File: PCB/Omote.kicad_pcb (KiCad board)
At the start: 2 copper layers, 192.4 x 50 mm, 158 parts, among them J1 USB_C_Receptacle_USB2.0, J2 Conn_01x50, J3 JST_PH_B2B-PH, J4 2.54x2 Header, Q1 DMG2301L, Q2 MBT3904DW1, Q3 DMG2301L, Q4 DMG2301L, Q5 DMG2301L, Q6 FS8205A, U1 DW01A, U10 APX803S, U11 TP4056, U2 XC6220B331, U3 CH340C, U4 USBLC6-2P6, U5 LIS3DHTR, U6 TSSP77038, U7 ESP32-PICO-D4, U8 AP2112K-3.3, U9 MAX17048G

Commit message: REV5 hardware added
TODO: update production files and BOMs
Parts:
- removed AE1: Antenna, omoteLib:RFANT5220110A2T
- removed C19: 1.2pF, Capacitor_SMD:C_0603_1608Metric
- removed kibuzzard-643EE532: G***, kibuzzard-643EE532
- removed kibuzzard-643EE5A3: G***, kibuzzard-643EE5A3
- added C29: 100nF, Capacitor_SMD:C_0603_1608Metric, F.Cu at (120.2, 116.9)
- added D10: LED, LED_SMD:LED_0603_1608Metric, B.Cu at (152.8, 91.9)
- added D11: LED, LED_SMD:LED_0603_1608Metric, B.Cu at (173.1, 91.8)
- added D12: LED, LED_SMD:LED_0603_1608Metric, B.Cu at (199.4, 117.0)
- added D13: LED, LED_SMD:LED_0603_1608Metric, B.Cu at (199.4, 102.0)
- added D14: LED, LED_SMD:LED_0603_1608Metric, B.Cu at (199.4, 87.0)
- added D15: LED, LED_SMD:LED_0603_1608Metric, B.Cu at (136.4, 102.0)
- added D16: LED, LED_SMD:LED_0603_1608Metric, B.Cu at (57.8, 124.2)
- added D6: LED, LED_SMD:LED_0603_1608Metric, B.Cu at (136.4, 89.7)
- added D7: LED, LED_SMD:LED_0603_1608Metric, B.Cu at (136.4, 114.3)
- added D8: LED, LED_SMD:LED_0603_1608Metric, B.Cu at (152.9, 112.0)
- added D9: LED, LED_SMD:LED_0603_1608Metric, B.Cu at (173.1, 112.0)
- added J5: Micro_SD_Card, omoteLib:MicroSD Slot TF-01A, F.Cu at (76.0, 116.0)
- added Q7: DMG2301L, Package_TO_SOT_SMD:SOT-23, F.Cu at (73.8, 105.2)
- added R10: 10k, Resistor_SMD:R_0603_1608Metric, F.Cu at (120.2, 115.4)
- added R2: 330, Resistor_SMD:R_0603_1608Metric, F.Cu at (72.8, 101.0)
- added R24: 10k, Resistor_SMD:R_0603_1608Metric, F.Cu at (72.8, 102.5)
- added R38: 2k2, Resistor_SMD:R_0603_1608Metric, B.Cu at (173.1, 93.3)
- added R41: 2k2, Resistor_SMD:R_0603_1608Metric, B.Cu at (199.4, 115.5)
- added R42: 2k2, Resistor_SMD:R_0603_1608Metric, B.Cu at (199.4, 100.5)
- added R43: 2k2, Resistor_SMD:R_0603_1608Metric, B.Cu at (199.4, 85.5)
- added R44: 2k2, Resistor_SMD:R_0603_1608Metric, F.Cu at (57.0, 123.2)
- added TP14: TestPoint, TestPoint:TestPoint_Pad_D1.5mm, F.Cu at (126.0, 112.5)
- added TP15: TestPoint, TestPoint:TestPoint_Pad_D1.5mm, F.Cu at (123.3, 112.5)
- added TP16: TestPoint, TestPoint:TestPoint_Pad_D1.5mm, F.Cu at (120.6, 112.5)
- added TP17: TestPoint, TestPoint:TestPoint_Pad_D1.5mm, B.Cu at (78.5, 108.7)
- added TP18: TestPoint, TestPoint:TestPoint_Pad_D1.5mm, B.Cu at (77.8, 111.2)
- added TP19: TestPoint, TestPoint:TestPoint_Pad_D1.5mm, B.Cu at (73.8, 108.7)
- added TP20: TestPoint, TestPoint:TestPoint_Pad_D1.5mm, B.Cu at (70.2, 110.0)
- added TP21: TestPoint, TestPoint:TestPoint_Pad_D1.5mm, B.Cu at (68.0, 121.2)
- added TP22: TestPoint, TestPoint:TestPoint_Pad_D1.5mm, B.Cu at (60.9, 124.2)
- added TP23: TestPoint, TestPoint:TestPoint_Pad_D1.5mm, B.Cu at (74.9, 111.5)
- added U12: TCA8418, Package_DFN_QFN:HVQFN-24-1EP_4x4mm_P0.5mm_EP2.5x2.5mm, F.Cu at (124.8, 118.1)
- C11: value 2.2uF -> 10uF; footprint Capacitor_SMD:C_0603_1608Metric -> Capacitor_SMD:C_0805_2012Metric
- C14: value 100nF -> 10uF; footprint Capacitor_SMD:C_0603_1608Metric -> Capacitor_SMD:C_0805_2012Metric
- C18: value 1.2pF -> 10uF; footprint Capacitor_SMD:C_0603_1608Metric -> Capacitor_SMD:C_0805_2012Metric
- D1: value MBR0520 -> BAT20J; footprint Diode_SMD:D_SOD-123 -> Diode_SMD:D_SOD-323
- D2: value SFH4547 -> SFH4547
- H4: footprint MountingHole:MountingHole_3.2mm_M3_Pad_Via -> MountingHole:MountingHole_3.2mm_M3
- R23, R31, R32, R33, R34, R35: value 10k -> 2k2; moved to B.Cu
- R36: value 0 -> 10k
- U7: value ESP32-PICO-D4 -> ESP32-S3-WROOM-1-N16R8; footprint omoteLib:QFN-48-1EP_7x7mm_P0.5mm_EP5.3x5.3mm_ThermalVias_MR -> RF_Module:ESP32-S3-WROOM-1
- moved R23 56.5 mm to (133.4, 102.0), turned to 0 degrees
- moved C14 51.6 mm to (116.8, 108.3), turned to -90 degrees
- moved FID4 43.4 mm to (54.7, 122.3)
- moved R34 42.0 mm to (173.1, 110.5)
- moved R31 35.4 mm to (133.4, 89.7)
- moved TP4 34.8 mm to (65.6, 80.6)
- moved FID3 34.7 mm to (239.4, 85.0)
- moved R35 32.7 mm to (152.8, 93.4), turned to 180 degrees
- moved TP3 32.6 mm to (67.9, 79.3)
- moved G*** 30.0 mm to (92.5, 117.8)
- moved R33 23.7 mm to (152.9, 110.5), turned to 180 degrees
- moved TP8 22.7 mm to (78.2, 105.8)
- moved R5 21.1 mm to (84.8, 82.5), turned to 180 degrees
- moved D3 20.5 mm to (81.7, 82.5)
- moved kibuzzard-643EE5B9 20.0 mm to (59.0, 122.8)
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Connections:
- net Net-(U3-V3) renamed USB_3V3
- C11 pad 1: +3.3V -> GND
- C11 pad 2: GND -> +3.3V
- C14 pad 1: +3.3V -> GND
- C14 pad 2: GND -> SW_BL
- C18 pad 2: Net-(U7-LNA_IN) -> /SD_3V3
- J2 pad 11: GND -> unconnected-(J2-Pin_11-Pad11)
- J2 pad 12: GND -> unconnected-(J2-Pin_12-Pad12)
- J2 pad 13: GND -> unconnected-(J2-Pin_13-Pad13)
- J2 pad 14: GND -> unconnected-(J2-Pin_14-Pad14)
- J2 pad 25: GND -> LCD_D7
- J2 pad 26: GND -> LCD_D6
- J2 pad 27: GND -> LCD_D5
- J2 pad 28: GND -> LCD_D4
- J2 pad 29: GND -> LCD_D3
- J2 pad 30: GND -> LCD_D2
- J2 pad 31: GND -> LCD_D1
- J2 pad 32: GND -> LCD_D0
- J2 pad 34: LCD_MOSI -> unconnected-(J2-Pin_34-Pad34)
- J2 pad 35: unconnected-(J2-Pin_35-Pad35) -> LCD_RD
- J2 pad 36: LCD_DC -> LCD_WR
- J2 pad 37: LCD_SCK -> LCD_DC
- J2 pad 7: +VSW -> GND
- J2 pad 8: +VSW -> GND
- J2 pad 9: +VSW -> GND
- R23 pad 1: CRG_STAT -> GND
- R23 pad 2: +3.3V -> Net-(D15-K)
- R31 pad 1: SW_A -> GND
- R31 pad 2: GND -> Net-(D6-K)
- R32 pad 1: SW_B -> GND
- R32 pad 2: GND -> Net-(D7-K)
- R33 pad 1: SW_C -> GND
- R33 pad 2: GND -> Net-(D8-K)
- R34 pad 1: SW_D -> GND
- R34 pad 2: GND -> Net-(D9-K)
- R35 pad 1: SW_E -> GND
- R35 pad 2: GND -> Net-(D10-K)
- R36 pad 1: Net-(AE1-A) -> TCA_INT
- R36 pad 2: Net-(U7-LNA_IN) -> +3.3V
- S17 pad 1: SW_2 -> GND
- S17 pad 2: SW_D -> SW_PWR
- U7 pad 1: +3.3V -> GND
- U7 pad 10: SW_D -> SD_MOSI
- U7 pad 11: SW_E -> SD_CS
- U7 pad 12: SW_1 -> TCA_INT
- U7 pad 13: IR_LED -> SCL
- U7 pad 14: IR_VCC -> SDA
- U7 pad 15: SW_2 -> unconnected-(U7-IO3-Pad15)
- U7 pad 16: SW_3 -> SW_BL
- U7 pad 17: SW_4 -> LCD_BL
- U7 pad 18: SW_5 -> LCD_D7
- U7 pad 19: +3.3V -> LCD_D6
- U7 pad 2: Net-(U7-LNA_IN) -> +3.3V
- U7 pad 20: ACC_INT -> LCD_D5
- U7 pad 21: IR_RX -> LCD_D4
- U7 pad 22: Net-(D3-A) -> LCD_D3
- U7 pad 23: IO0 -> LCD_D2
- U7 pad 24: LCD_BL -> LCD_D1
- U7 pad 25: unconnected-(U7-IO16-Pad25) -> LCD_D0
- U7 pad 26: unconnected-(U7-VDD_SDIO-Pad26) -> Net-(D3-A)
- U7 pad 27: unconnected-(U7-IO17-Pad27) -> IO0
- U7 pad 28: LCD_DC -> unconnected-(U7-IO35-Pad28)
- U7 pad 29: LCD_EN -> unconnected-(U7-IO36-Pad29)
- U7 pad 3: +3.3V -> ESP_EN
- U7 pad 31: unconnected-(U7-CLK-Pad31) -> LCD_EN
- U7 pad 32: unconnected-(U7-SD0-Pad32) -> LCD_CS
- U7 pad 33: unconnected-(U7-SD1-Pad33) -> LCD_DC
- U7 pad 34: LCD_CS -> LCD_WR
- U7 pad 35: LCD_SCK -> LCD_RD
- U7 pad 36: LCD_MOSI -> USB_RXD
- U7 pad 37: +3.3V -> USB_TXD
- U7 pad 38: SDA -> ACC_INT
- U7 pad 39: SCL -> CRG_STAT
- U7 pad 4: +3.3V -> IR_RX
- U7 pad 40: USB_RXD -> GND
- U7 pad 41: USB_TXD -> GND
- U7 pad 5: unconnected-(U7-SENSOR_VP-Pad5) -> IR_LED
- U7 pad 6: SW_A -> IR_VCC
- U7 pad 7: SW_B -> SD_MISO
- U7 pad 8: SW_C -> SD_SCK
- U7 pad 9: ESP_EN -> SD_EN
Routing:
- net SW_BL: track 0.00 -> 343.4 mm, vias 0 -> 5
- net USB_3V3: track 18.9 -> 123.3 mm, vias 0 -> 2
- net SW_D: track 171.7 -> 73.8 mm, vias 2 -> 1
- net SW_2: track 173.8 -> 80.4 mm, vias 2 -> 1
- net SW_C: track 232.7 -> 145.0 mm
- net SW_B: track 167.9 -> 81.6 mm
- net SW_A: track 211.6 -> 126.6 mm
- net SW_E: track 135.9 -> 55.9 mm
- net SW_1: track 159.4 -> 84.3 mm
- net SW_3: track 169.4 -> 95.6 mm
- net SD_DET: track 0.00 -> 71.4 mm, vias 0 -> 1
- net SW_PWR: track 0.00 -> 69.9 mm, vias 0 -> 1
- net SW_4: track 167.3 -> 97.7 mm
- net SW_5: track 187.4 -> 120.9 mm
- net SCL: track 178.5 -> 244.9 mm, vias 3 -> 5
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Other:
- outline, holes or cut-outs redrawn
- board text added: "OMOTE Rev. 5 Maximilian Kern 12/2024"
- board text removed: "OMOTE Rev. 4 Maximilian Kern 04/2024"

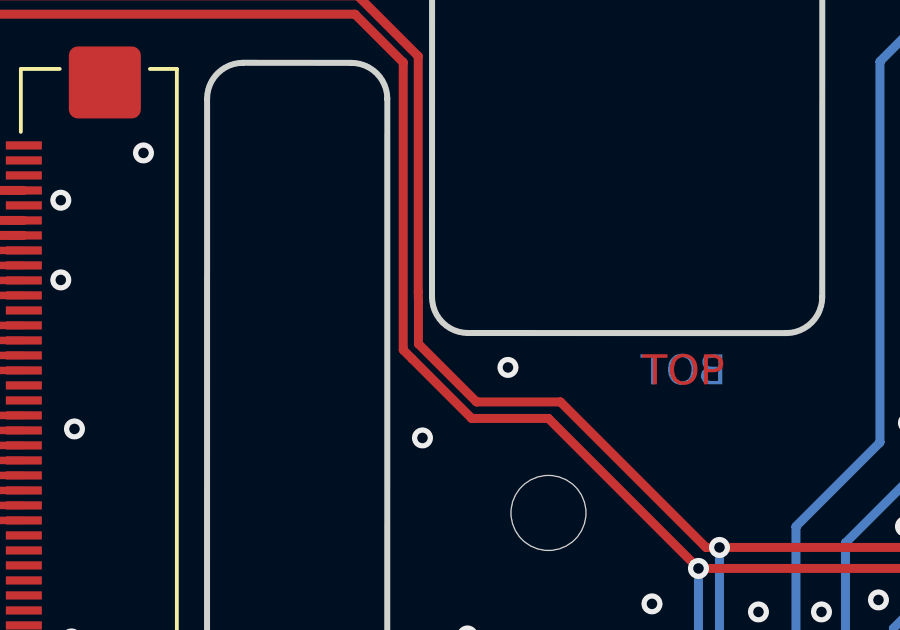
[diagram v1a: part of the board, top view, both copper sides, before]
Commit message: Fixed LCSC number for R7/R9
The LCSC part number  for R7 and R9 was wrongly linked to a 5.1 Ohm resistor instead of a 5.1 KiloOhm resistor.
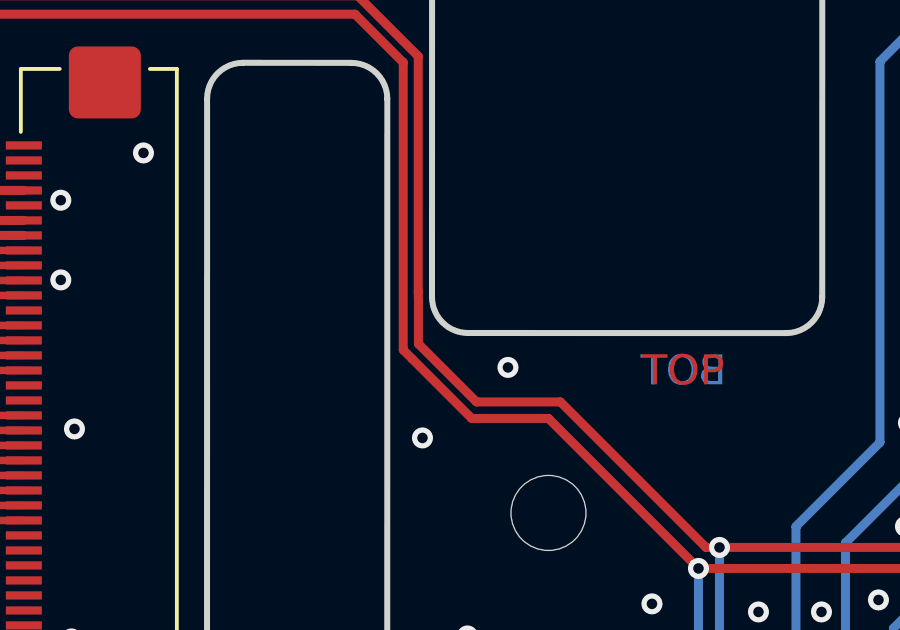
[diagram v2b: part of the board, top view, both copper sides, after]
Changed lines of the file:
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@@
 		(fp_arc
 			(start 5.997926 25.19481)
-			(mid 6.349398 24.346284)
+			(mid 6.349398 24.34628)
 			(end 7.197926 23.99481)
 			(stroke
@@
 			(pinfunction "1")
 			(pintype "input")
+			(zone_connect 2)
 		)
 		(pad "1" thru_hole circle
@@
 			)
 		)
-		(property "LCSC" "C114626"
+		(property "LCSC" "C105580"
 			(at 0 0 90)
 			(unlocked yes)
@@
 			)
 		)
-		(property "LCSC" "C114626"
+		(property "LCSC" "C105580"
 			(at 0 0 0)
 			(unlocked yes)
@@
 			)
 		)
-		(property "LCSC" "C965807"
+		(property "LCSC" "C84265"
 			(at 0 0 180)
 			(unlocked yes)
@@
 			)
 		)
-		(property "LCSC" "C965807"
+		(property "LCSC" "C84265"
 			(at 0 0 0)
 			(unlocked yes)
@@
 			)
 		)
-		(property "LCSC" "C965807"
+		(property "LCSC" "C84265"
 			(at 0 0 0)
 			(unlocked yes)
@@
 			)
 		)
-		(property "LCSC" "C965807"
+		(property "LCSC" "C84265"
 			(at 0 0 180)
 			(unlocked yes)
@@
 			)
 		)
-		(property "LCSC" "C965807"
+		(property "LCSC" "C84265"
 			(at 0 0 180)
 			(unlocked yes)
@@
 			)
 		)
-		(property "LCSC" "C965807"
+		(property "LCSC" "C84265"
 			(at 0 0 0)
 			(unlocked yes)
@@
 			)
 		)
-		(property "LCSC" "C965807"
+		(property "LCSC" "C84265"
 			(at 0 0 180)
 			(unlocked yes)
@@
 			)
 		)
-		(property "LCSC" "C965807"
+		(property "LCSC" "C84265"
 			(at 0 0 0)
 			(unlocked yes)
@@
 			)
 		)
-		(property "LCSC" "C965807"
+		(property "LCSC" "C84265"
 			(at 0 0 180)
 			(unlocked yes)
@@
 			)
 		)
-		(property "LCSC" "C965807"
+		(property "LCSC" "C84265"
 			(at 0 0 0)
 			(unlocked yes)
@@
 			)
 		)
-		(property "LCSC" "C965807"
+		(property "LCSC" "C84265"
 			(at 0 0 180)
 			(unlocked yes)

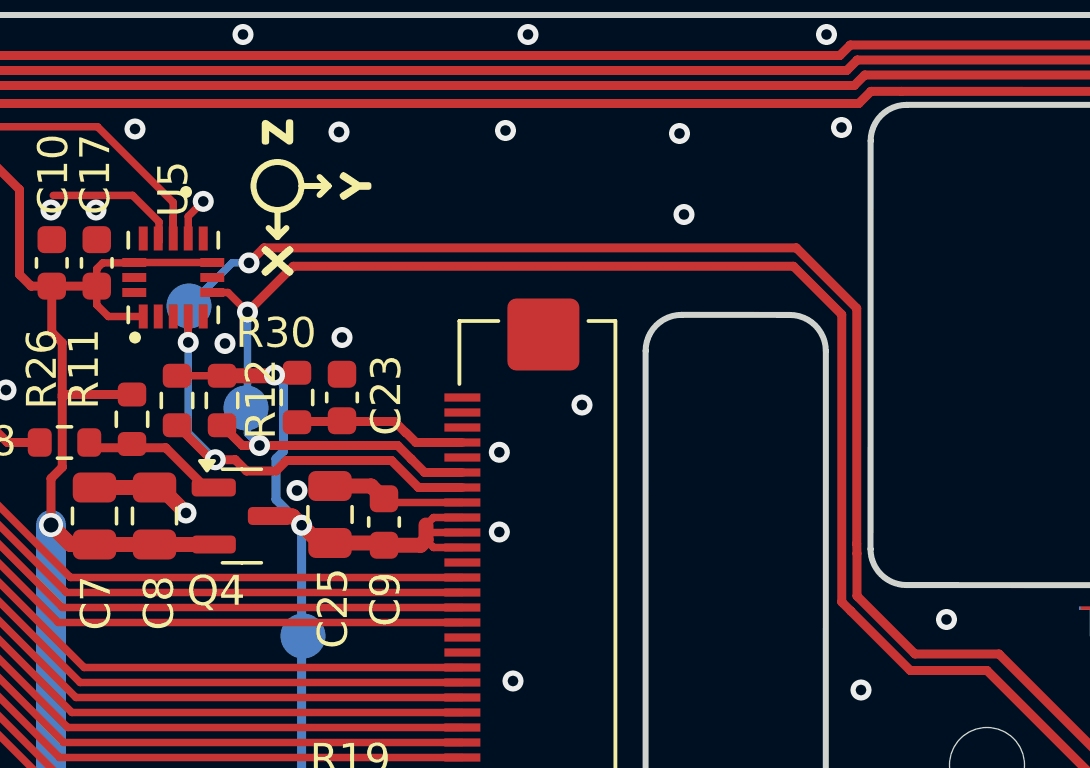
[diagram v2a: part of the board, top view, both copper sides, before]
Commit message: MOSFET circuit adjustment
- Increased gate resistors from 330Ohm to 1kOhm to lower edge speeds slightly (not absolutely necessary but 1k seems to be a default value for most display eval boards)
- Set R25 (gate pull-up for backlight) to 10kOhm like all others
- Removed C14 to reduce load on the ESP32 pin
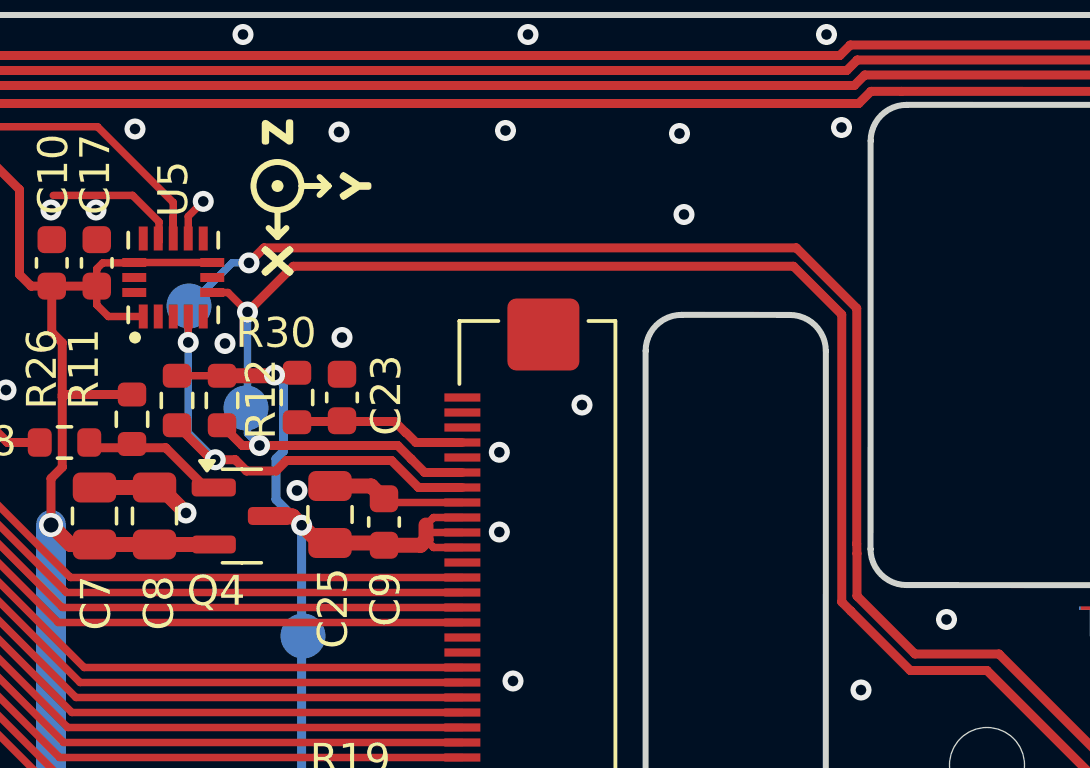
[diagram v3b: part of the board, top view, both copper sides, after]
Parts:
- R2, R27, R28, R29: value 330 -> 1k
- R25: value 4k7 -> 10k
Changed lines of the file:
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@@
 			)
 		)
-		(property "Value" "4k7"
+		(property "Value" "10k"
 			(at 0 1.43 0)
 			(layer "F.Fab")
@@
 			)
 		)
-		(property "LCSC" "C99782"
+		(property "LCSC" "C98220"
 			(at 0 0 180)
 			(unlocked yes)
@@
 		(sheetname "Root")
 		(sheetfile "Omote.kicad_sch")
+		(zone_connect 2)
 		(attr exclude_from_pos_files exclude_from_bom)
 		(fp_circle
@@
 		(fp_arc
 			(start 5.997926 25.19481)
-			(mid 6.349398 24.34628)
+			(mid 6.349398 24.346284)
 			(end 7.197926 23.99481)
 			(stroke
@@
 		(sheetname "Root")
 		(sheetfile "Omote.kicad_sch")
-		(attr smd)
+		(attr smd exclude_from_bom dnp)
 		(fp_line
 			(start -0.261252 0.735)
@@
 			)
 		)
-		(property "Value" "330"
+		(property "Value" "1k"
 			(at 0 1.43 0)
 			(layer "F.Fab")
@@
 			)
 		)
-		(property "LCSC" "C105881"
+		(property "LCSC" "C22548"
 			(at 0 0 0)
 			(unlocked yes)
@@
 			)
 		)
-		(property "Value" "330"
+		(property "Value" "1k"
 			(at 0 1.43 0)
 			(layer "F.Fab")
@@
 			)
 		)
-		(property "LCSC" "C105881"
+		(property "LCSC" "C22548"
 			(at 0 0 180)
 			(unlocked yes)
@@
 		(sheetname "Root")
 		(sheetfile "Omote.kicad_sch")
+		(zone_connect 2)
 		(attr exclude_from_pos_files exclude_from_bom)
 		(fp_circle
@@
 			)
 		)
-		(property "Value" "330"
+		(property "Value" "1k"
 			(at 0 1.43 0)
 			(layer "F.Fab")
@@
 			)
 		)
-		(property "LCSC" "C105881"
+		(property "LCSC" "C22548"
 			(at 0 0 180)
 			(unlocked yes)
@@
 		(sheetname "Root")
 		(sheetfile "Omote.kicad_sch")
+		(zone_connect 2)
 		(attr exclude_from_pos_files exclude_from_bom)
 		(fp_circle
@@
 			)
 		)
-		(property "Value" "330"
+		(property "Value" "1k"
 			(at 0 1.43 0)
 			(layer "F.Fab")
@@
 			)
 		)
-		(property "LCSC" "C105881"
+		(property "LCSC" "C22548"
 			(at 0 0 180)
 			(unlocked yes)
@@
 		(sheetname "Root")
 		(sheetfile "Omote.kicad_sch")
+		(zone_connect 2)
 		(attr exclude_from_pos_files exclude_from_bom)
 		(fp_circle
@@
 	)
 	(gr_circle
-		(center 92.8 82.9)
-		(end 92.9 82.9)
+		(center 95.85 82.7)
+		(end 95.95 82.7)
 		(stroke
 			(width 0.2)
